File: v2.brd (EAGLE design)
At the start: 24 x 24 mm, 47 parts, among them Q1 12MHz, T1 BSS84

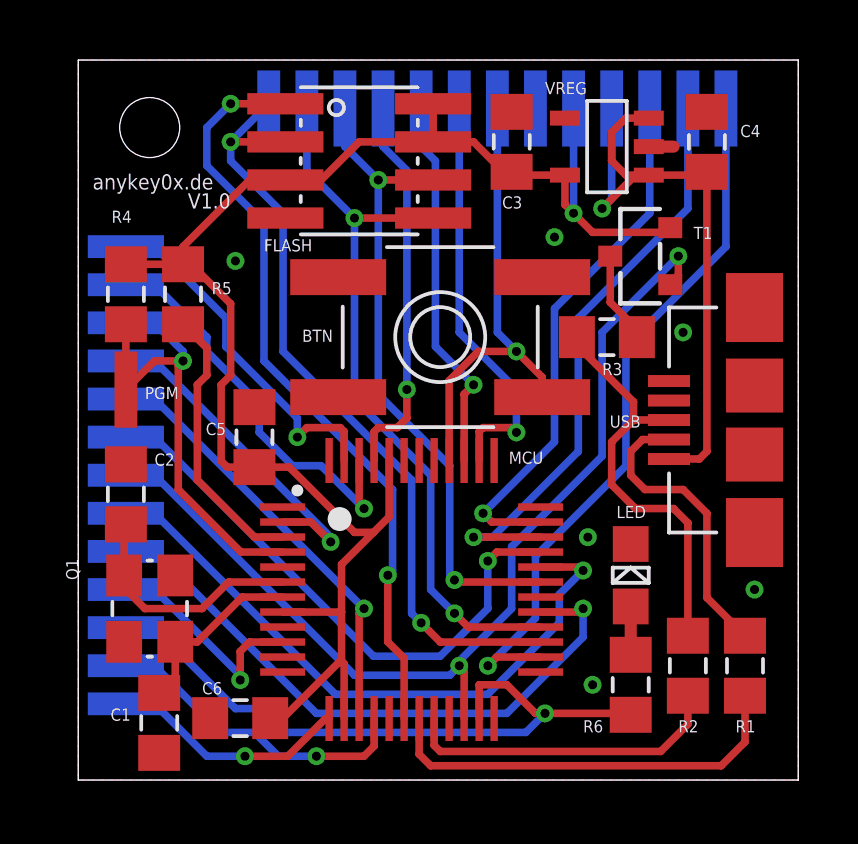
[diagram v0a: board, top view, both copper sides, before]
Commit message: Lessons learned: Larger font, reversed USB Pullup, clearer silkscreen, wider and rounded solder pads
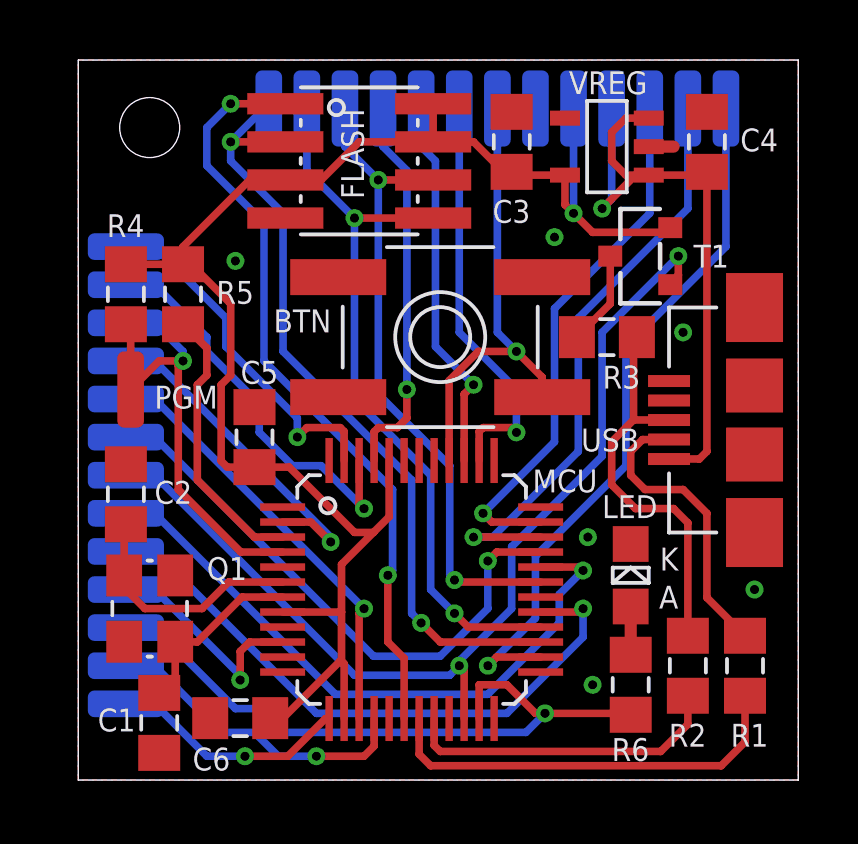
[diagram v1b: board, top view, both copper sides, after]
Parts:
- moved PGM 0.16 mm to (1.75, 13.0)
- turned R3 to 0 degrees
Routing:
- net USB_D+: track 14.4 -> 13.3 mm
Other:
- board text added: "A"
- board text added: "K"
- board text added: "PRESS ANY KEY."
- board text added: "V1.1"
- board text removed: "V1.0"
